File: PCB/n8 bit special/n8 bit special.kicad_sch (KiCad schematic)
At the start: 45 parts, among them J1 USB_B_Micro, J2 PORT0, J3 PORT1, J4 PORT2, J6 Conn_02x08_Odd_Even, Q1 2N3904, SW1 SW_Push_Dual, U1 W65C02SxP, U10 74HC00, U2 CY62256-70PC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

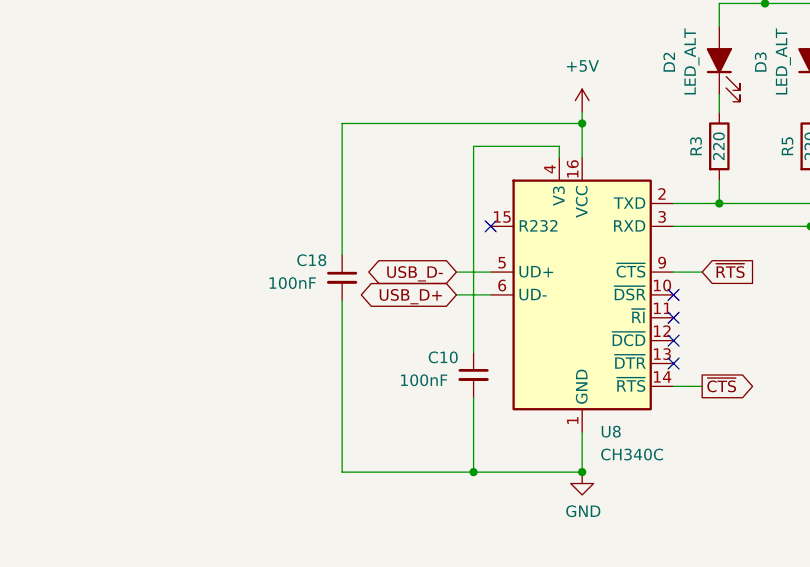
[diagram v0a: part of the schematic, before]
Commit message: Fixed D+/D- miswiring
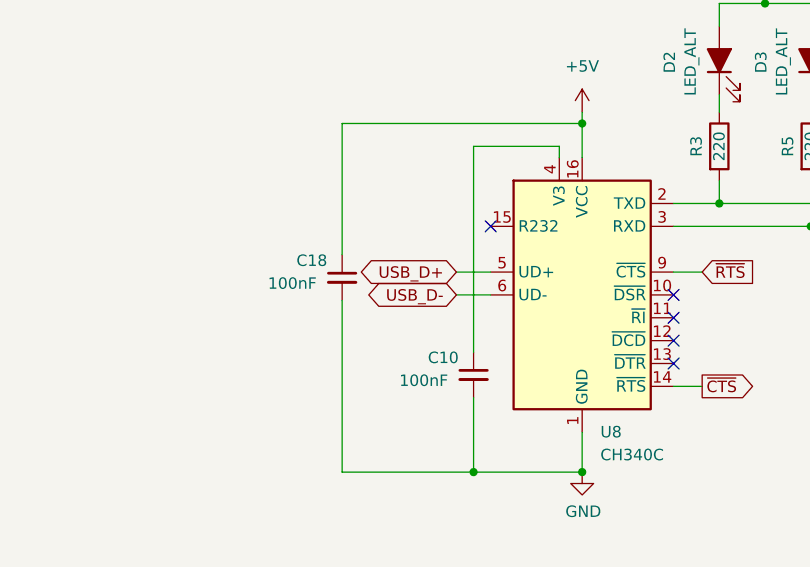
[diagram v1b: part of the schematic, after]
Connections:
- net USB_D+: now also U8.5 (UD+); no longer U8.6 (UD-)
- net USB_D-: now also U8.6 (UD-); no longer U8.5 (UD+)

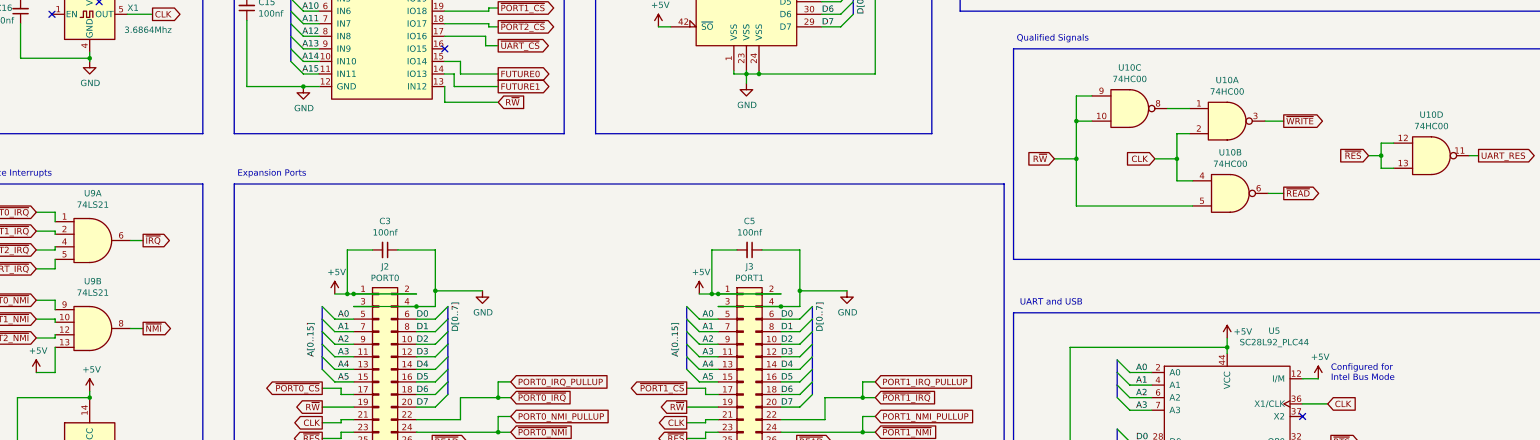
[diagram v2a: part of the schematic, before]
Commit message: added 2 new soundcard designs
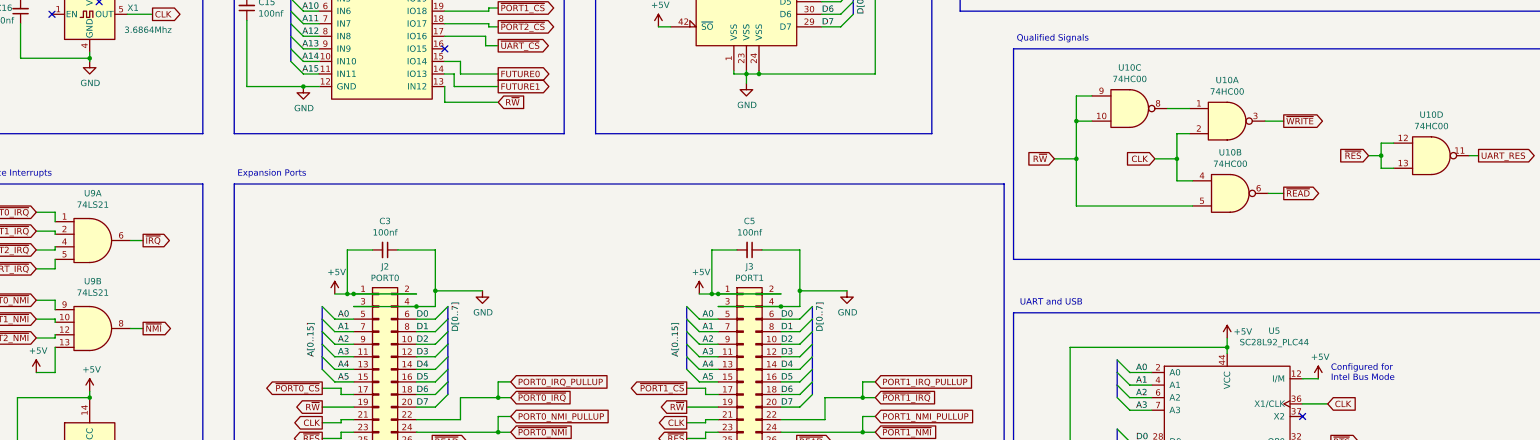
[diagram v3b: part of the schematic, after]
